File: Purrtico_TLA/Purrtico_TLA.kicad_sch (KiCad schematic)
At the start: 66 parts, among them J1 XLR3, J2 Conn_01x03, J3 Conn_01x02, J4 XLR3, J5 Conn_01x02, U1 OPA1679, U2 OPA1679

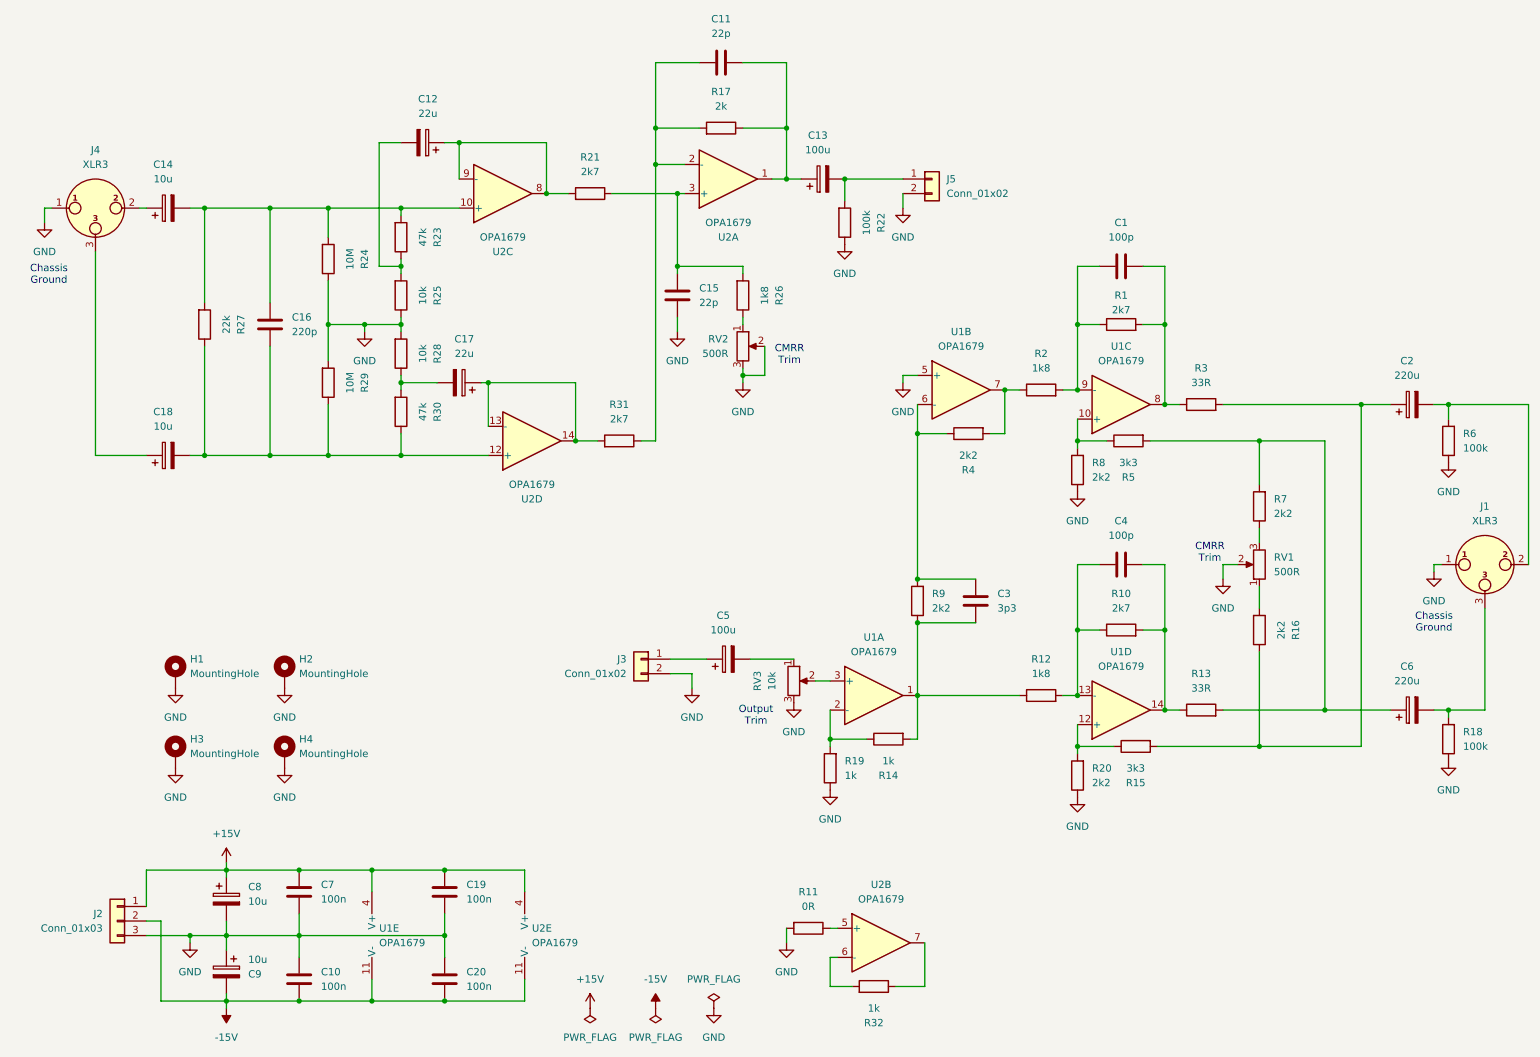
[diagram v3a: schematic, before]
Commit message: started purrtico m eq
singla band only, for testing
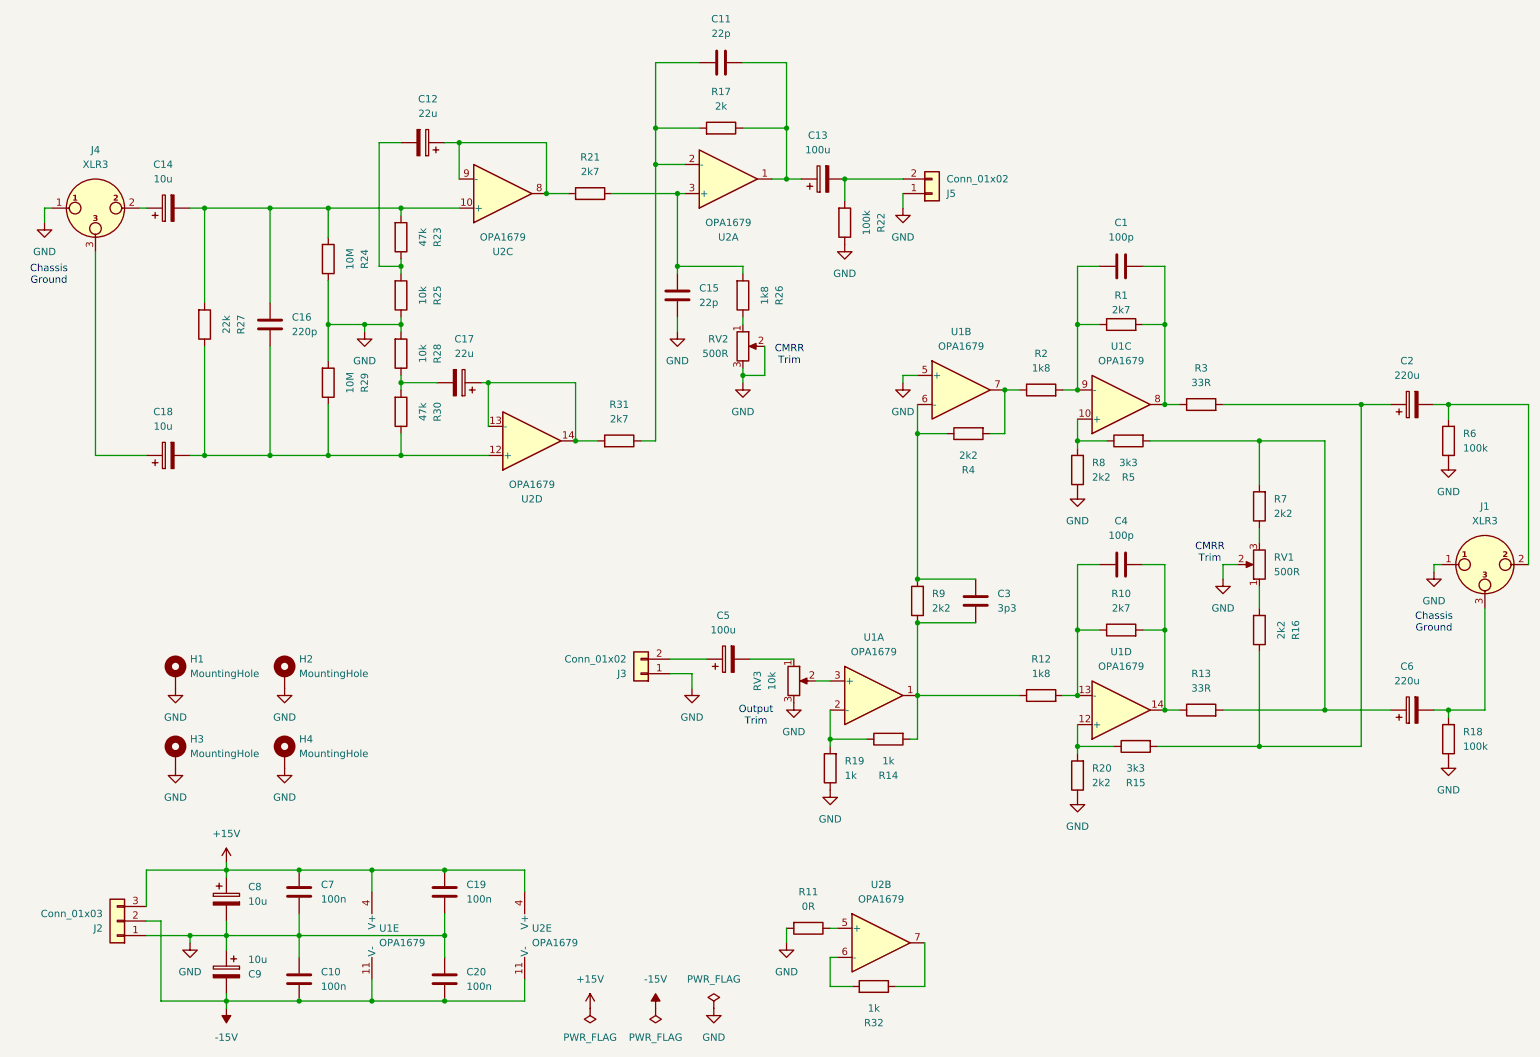
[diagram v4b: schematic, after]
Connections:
- net +15V: now also J2.3 (Pin_3); no longer J2.1 (Pin_1)
- net GND: now also J2.1 (Pin_1), J3.1 (Pin_1), J5.1 (Pin_1); no longer J2.3 (Pin_3), J3.2 (Pin_2), J5.2 (Pin_2)
- net at C13.2, R22.2: now also J5.2 (Pin_2); no longer J5.1 (Pin_1)
- net at C5.1: now also J3.2 (Pin_2); no longer J3.1 (Pin_1)
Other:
- moved on the sheet: J2, J3
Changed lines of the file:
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@@
 	(title_block
 		(title "Purrtico TLA Input & Output")
-		(date "2024-05-30")
+		(date "2024-07-18")
 		(rev "01")
 		(company "Greybox Audio")
@@
 	(symbol
 		(lib_id "Connector_Generic:Conn_01x02")
-		(at 121.92 128.27 0)
-		(mirror y)
+		(at 121.92 130.81 180)
 		(unit 1)
 		(exclude_from_sim no)
@@
 		(dnp no)
 		(property "Reference" "J3"
-			(at 119.38 128.2699 0)
+			(at 119.38 130.8101 0)
 			(effects
 				(font
@@
 		)
 		(property "Value" "Conn_01x02"
-			(at 119.38 130.8099 0)
+			(at 119.38 128.2701 0)
 			(effects
 				(font
@@
 		)
 		(property "Footprint" "Connector_PinHeader_2.54mm:PinHeader_1x02_P2.54mm_Vertical"
-			(at 121.92 128.27 0)
+			(at 121.92 130.81 0)
 			(effects
 				(font
@@
 		)
 		(property "Datasheet" "~"
-			(at 121.92 128.27 0)
+			(at 121.92 130.81 0)
 			(effects
 				(font
@@
 		)
 		(property "Description" "Generic connector, single row, 01x02, script generated (kicad-library-utils/schlib/autogen/connector/)"
-			(at 121.92 128.27 0)
+			(at 121.92 130.81 0)
 			(effects
 				(font
@@
 	(symbol
 		(lib_id "Connector_Generic:Conn_01x03")
-		(at 30.48 173.99 0)
-		(mirror y)
+		(at 30.48 173.99 180)
 		(unit 1)
 		(exclude_from_sim no)
@@
 		(dnp no)
 		(property "Reference" "J2"
-			(at 27.94 172.7199 0)
+			(at 27.94 175.2601 0)
 			(effects
 				(font
@@
 		)
 		(property "Value" "Conn_01x03"
-			(at 27.94 175.2599 0)
+			(at 27.94 172.7201 0)
 			(effects
 				(font
@@
 	(symbol
 		(lib_id "Connector_Generic:Conn_01x02")
-		(at 172.72 44.45 0)
+		(at 172.72 46.99 0)
+		(mirror x)
 		(unit 1)
 		(exclude_from_sim no)
@@
 		(dnp no)
 		(property "Reference" "J5"
-			(at 175.26 44.4499 0)
+			(at 175.26 46.9901 0)
 			(effects
 				(font
@@
 		)
 		(property "Value" "Conn_01x02"
-			(at 175.26 46.9899 0)
+			(at 175.26 44.4501 0)
 			(effects
 				(font
@@
 		)
 		(property "Footprint" "Connector_PinHeader_2.54mm:PinHeader_1x02_P2.54mm_Vertical"
-			(at 172.72 44.45 0)
+			(at 172.72 46.99 0)
 			(effects
 				(font
@@
 		)
 		(property "Datasheet" "~"
-			(at 172.72 44.45 0)
+			(at 172.72 46.99 0)
 			(effects
 				(font
@@
 		)
 		(property "Description" "Generic connector, single row, 01x02, script generated (kicad-library-utils/schlib/autogen/connector/)"
-			(at 172.72 44.45 0)
+			(at 172.72 46.99 0)
 			(effects
 				(font

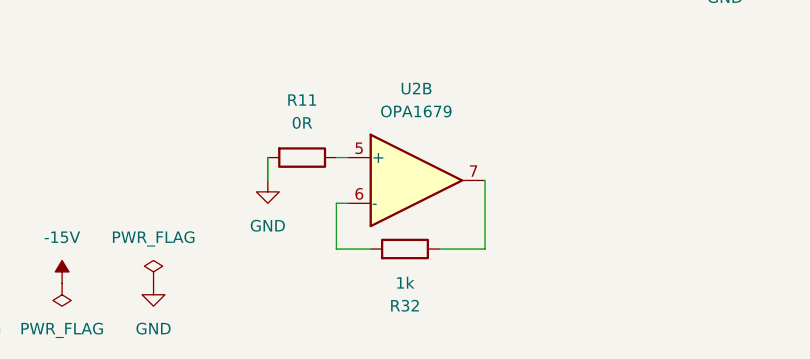
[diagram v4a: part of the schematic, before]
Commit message: update 0R resistors
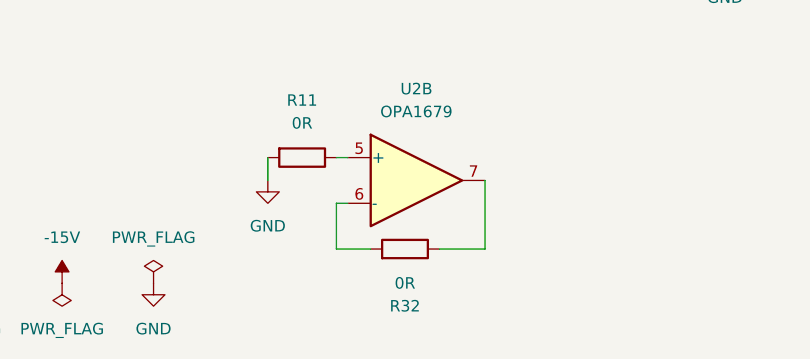
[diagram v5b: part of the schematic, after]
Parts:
- R32: value 1k -> 0R
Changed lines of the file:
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@@
 	)
 	(symbol
+		(lib_id "Device:R")
+		(at 162.56 185.42 270)
+		(mirror x)
+		(unit 1)
+		(exclude_from_sim no)
+		(in_bom yes)
+		(on_board yes)
+		(dnp no)
+		(property "Reference" "R32"
+			(at 162.56 191.77 90)
+			(effects
+				(font
+					(size 1.27 1.27)
+				)
+			)
+		)
+		(property "Value" "0R"
+			(at 162.56 189.23 90)
+			(effects
+				(font
+					(size 1.27 1.27)
+				)
+			)
+		)
+		(property "Footprint" "Resistor_SMD:R_1206_3216Metric"
+			(at 162.56 187.198 90)
+			(effects
+				(font
+					(size 1.27 1.27)
+				)
+				(hide yes)
+			)
+		)
+		(property "Datasheet" "~"
+			(at 162.56 185.42 0)
+			(effects
+				(font
+					(size 1.27 1.27)
+				)
+				(hide yes)
+			)
+		)
+		(property "Description" ""
+			(at 162.56 185.42 0)
+			(effects
+				(font
+					(size 1.27 1.27)
+				)
+				(hide yes)
+			)
+		)
+		(pin "1"
+		)
+		(pin "2"
+		)
+		(instances
+			(project "Purrtico_TLA"
+				(path "/8744b698-520b-403d-9dc8-5ad840d7038f"
+					(reference "R32")
+					(unit 1)
+				)
+			)
+		)
+	)
+	(symbol
 		(lib_id "Amplifier_Operational:OPA1679")
 		(at 177.8 81.28 0)
@@
 	)
 	(symbol
-		(lib_id "Device:R")
-		(at 162.56 185.42 270)
-		(mirror x)
-		(unit 1)
-		(exclude_from_sim no)
-		(in_bom yes)
-		(on_board yes)
-		(dnp no)
-		(property "Reference" "R32"
-			(at 162.56 191.77 90)
-			(effects
-				(font
-					(size 1.27 1.27)
-				)
-			)
-		)
-		(property "Value" "1k"
-			(at 162.56 189.23 90)
-			(effects
-				(font
-					(size 1.27 1.27)
-				)
-			)
-		)
-		(property "Footprint" "Resistor_SMD:R_1206_3216Metric"
-			(at 162.56 187.198 90)
-			(effects
-				(font
-					(size 1.27 1.27)
-				)
-				(hide yes)
-			)
-		)
-		(property "Datasheet" "~"
-			(at 162.56 185.42 0)
-			(effects
-				(font
-					(size 1.27 1.27)
-				)
-				(hide yes)
-			)
-		)
-		(property "Description" ""
-			(at 162.56 185.42 0)
-			(effects
-				(font
-					(size 1.27 1.27)
-				)
-				(hide yes)
-			)
-		)
-		(pin "1"
-		)
-		(pin "2"
-		)
-		(instances
-			(project "Purrtico_TLA"
-				(path "/8744b698-520b-403d-9dc8-5ad840d7038f"
-					(reference "R32")
-					(unit 1)
-				)
-			)
-		)
-	)
-	(symbol
 		(lib_id "power:PWR_FLAG")
 		(at 113.03 189.23 0)
@@
 			)
 		)
-		(property "Datasheet" " ~"
+		(property "Datasheet" "~"
 			(at 26.67 49.53 0)
 			(effects
@@
 			)
 		)
-		(property "Datasheet" " ~"
+		(property "Datasheet" "~"
 			(at 269.24 111.76 0)
 			(effects

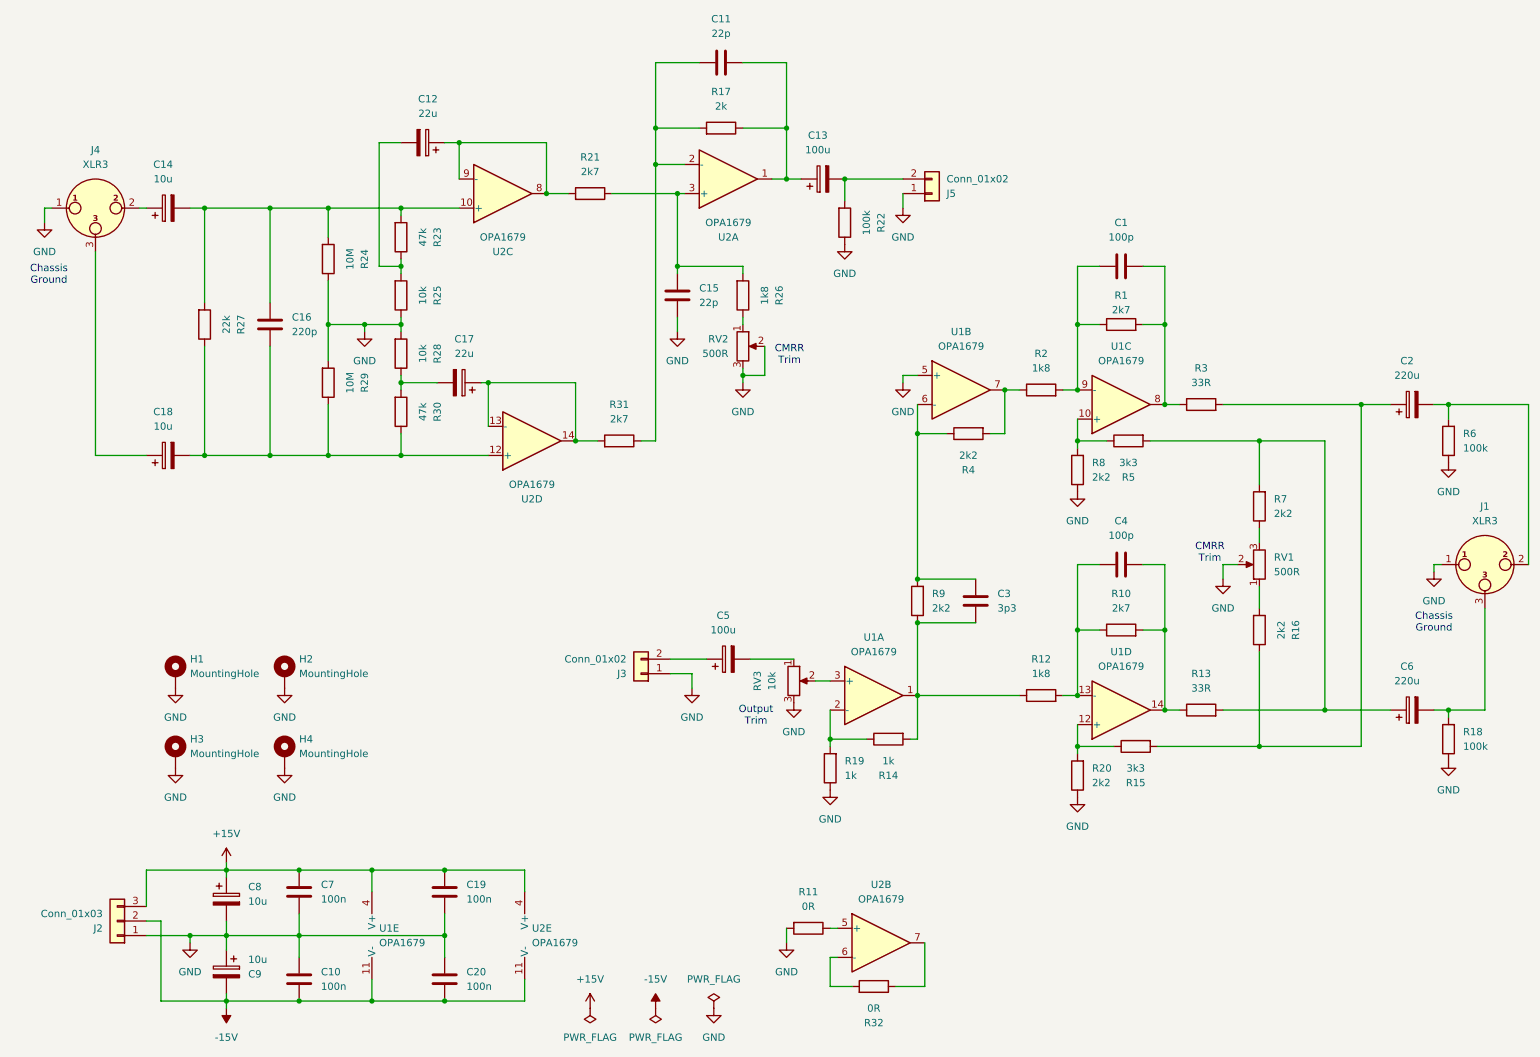
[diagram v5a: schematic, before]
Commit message: update pcb
swapped position of input/output, replaced power connector with a 10pin eurorack connector
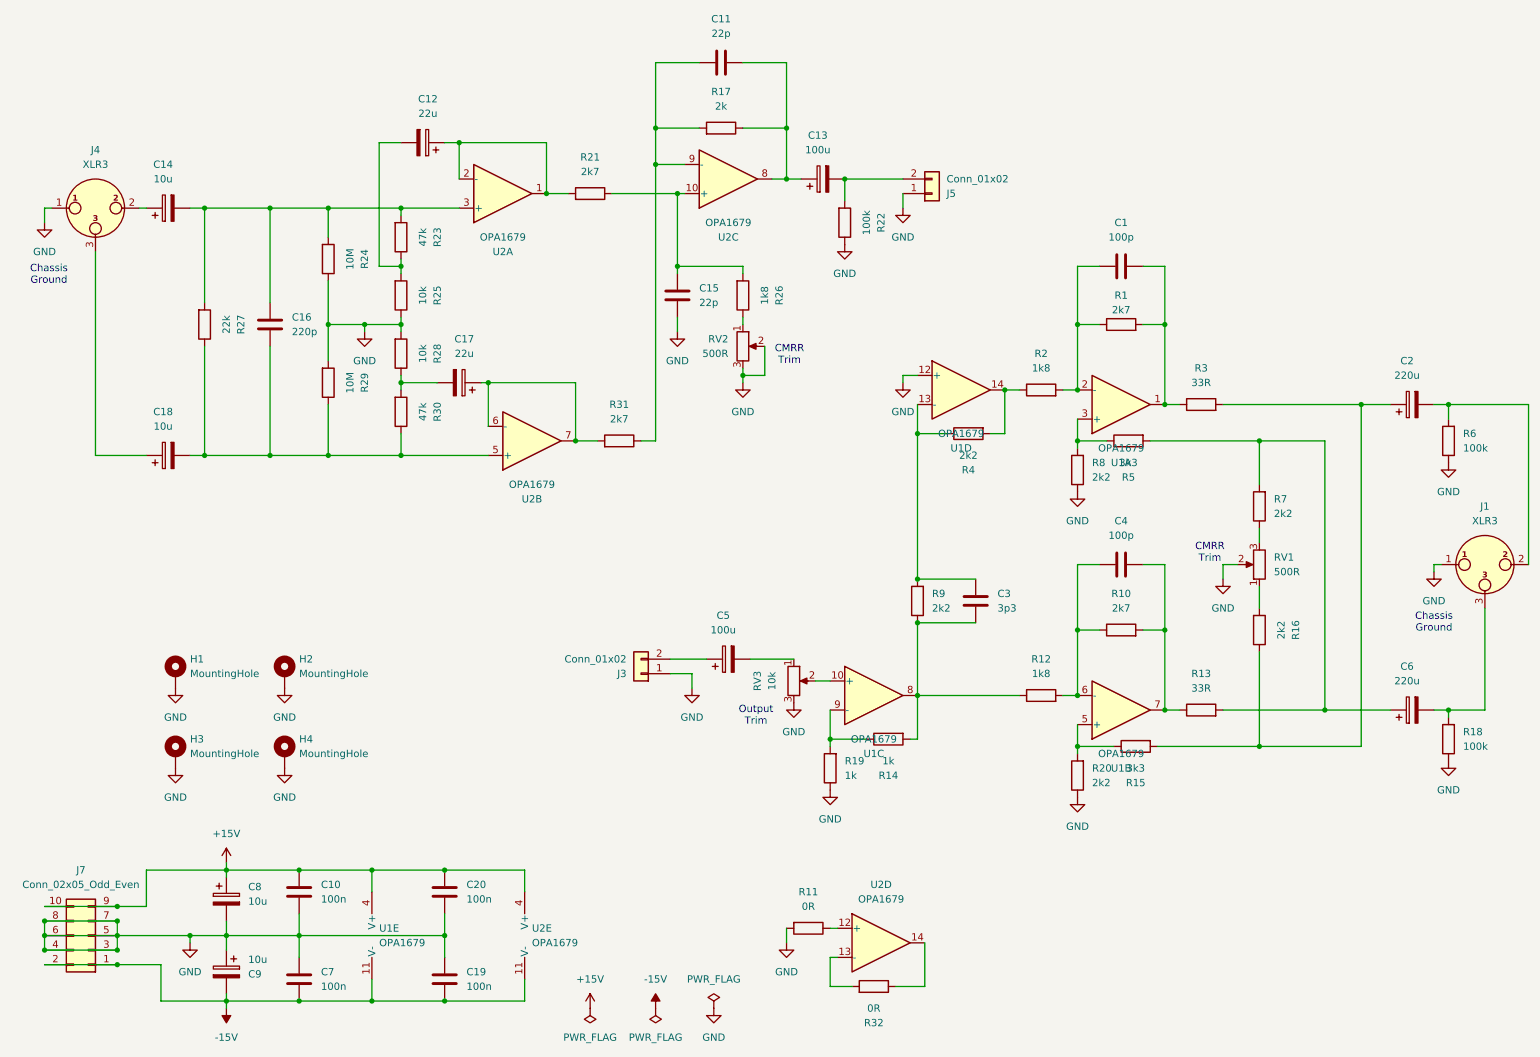
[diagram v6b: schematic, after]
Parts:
- removed J2: Conn_01x03, Connector_PinHeader_2.54mm:PinHeader_1x03_P2.54mm_Vertical, symbol Connector_Generic:Conn_01x03
- added J7: Conn_02x05_Odd_Even, Connector_PinHeader_2.54mm:PinHeader_2x05_P2.54mm_Vertical, symbol Connector_Generic:Conn_02x05_Odd_Even
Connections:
- net +15V: now also C10.2, C20.2, J7.10 (Pin_10), J7.9 (Pin_9); no longer C19.1, C7.1
- net -15V: now also C19.1, C7.1, J7.1 (Pin_1), J7.2 (Pin_2); no longer C10.2, C20.2
- net GND: now also U1.12 (+), J7.3 (Pin_3), J7.4 (Pin_4), J7.5 (Pin_5), J7.6 (Pin_6), J7.7 (Pin_7), J7.8 (Pin_8); no longer U1.5 (+)
- net at C11.1, C13.1, R17.1: now also U2.8; no longer U2.1
- net at R5.1, R8.2: now also U1.3 (+); no longer U1.10 (+)
- net at C1.2, R1.2, R3.1: now also U1.1; no longer U1.8
- net at C1.1, R1.1, R2.2: now also U1.2 (-); no longer U1.9 (-)
- net at C4.1, R10.1, R12.2: now also U1.6 (-); no longer U1.13 (-)
- net at C4.2, R10.2, R13.1: now also U1.7; no longer U1.14
- net at C14.2, C16.2, R23.2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: now also U2.3 (+); no longer U2.10 (+)
- net at C16.1, C18.2, R27.1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: now also U2.5 (+); no longer U2.12 (+)
- net at C3.1, R12.1, R14.2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: now also U1.8; no longer U1.1
- net at R14.1, R19.2: now also U1.9 (-); no longer U1.2 (-)
- net at RV3.2: now also U1.10 (+); no longer U1.3 (+)
- net at C12.1, R21.2: now also U2.1, U2.2 (-); no longer U2.8, U2.9 (-)
- net at R11.1: now also U2.12 (+); no longer U2.5 (+)
- net at C11.2, R17.2, R31.1: now also U2.9 (-); no longer U2.2 (-)
- net at R15.1, R20.2: now also U1.5 (+); no longer U1.12 (+)
- net at C17.1, R31.2: now also U2.6 (-), U2.7; no longer U2.13 (-), U2.14
- net at C3.2, R4.1, R9.2: now also U1.13 (-); no longer U1.6 (-)
- net at R32.1: now also U2.14; no longer U2.7
- net at R32.2: now also U2.13 (-); no longer U2.6 (-)
- net at R2.1, R4.2: now also U1.14; no longer U1.7
- net at C15.1, R21.1, R26.2: now also U2.10 (+); no longer U2.3 (+)
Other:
- moved on the sheet: C10, C19, C20, C7, U1A, U1B, U1C, U1D, U2A, U2B, U2C, U2D
